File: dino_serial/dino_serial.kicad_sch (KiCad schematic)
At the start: 0 parts

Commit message: feat: phase G on silicon -- serial card, 9600 8N1, echo proven
The PC16550D card (U101 '138, U102 '245, U103, dino_serial/) runs on the
bench. Every step-4..8 witness passed 2026-09-04: serid 0x55, serid_aa
0xAA, serlsr 0x60, seriir 0xC1, serbaud 153.6 kHz on U103.15, serloop
0x53, sertx "DINO" on the host terminal, serrx echoing a typed character
on OB and back to the host. The data bus is PROVEN, not narrowed: a
receiver DINO does not control decoded it.

Two bench faults found and fixed on the way, both copper, neither
visible to --continuity:
  - the card's ~WR was on U75.5 (an input) instead of U75.6; ~{IO_WR}
    now feeds a real consumer for the first time.
  - C1 was 1uF in the socket against 10uF in the drawing, so the machine
    had no power-on reset: reset released ~1ms into the rail ramp and the
    UART started un-reset, framing 5-bit characters until the button
    gave it its first real MR. 10uF fitted; cold boot is clean. New rule
    in CLAUDE.md: a component value is copper too.

Tooling:
  - progrom_gen.Unoracled: the oracle's by-design refusals (non-SCR UART
    registers, undefined carry) are a subclass; asm.py --run reports them
    and still writes the image instead of dying in make burn-prog-*.
    roms_readme_gen lists such images as UNORACLED.
  - docs/notes/serprobe_host.py: stdlib host probe, sends bytes and prints
    every returned byte in hex with timing. Replaces the terminal as the
    serial witness.
  - docs/notes/test_serial_card.py: the card schematic's paper witness.
  - Makefile: make monitor / kill-monitor.

Images: the eight phase G witnesses, five diagnostics from the cold-boot
chase (serrx0, serlcr, serlive, serrxlcr, serrxlive), and the phase F
coverage ROMs that were on disk but never committed.

Co-Authored-By: Claude Fable 5.1 <noreply@anthropic.com>
Claude-Session: https://claude.ai/code/session_01WMy1UioY1p8BufsC2zZ3hR
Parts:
- added C1, C2, C3: 0.1µF, symbol Device:C_Small
- added J1: FTDI I/O, symbol Connector:Conn_01x06_Socket
- added U101: 74LS138, symbol 74xx:74LS138
- added U102: 74LS245, symbol 74xx:74LS245
- added U103: 16550, Package_DIP:DIP-40_W15.24mm, symbol Interface_UART:16550
- added Y1: 3.6864MHz, Oscillator:Oscillator_DIP-8, symbol Oscillator:CXO_DIP8
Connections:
- new net +5V: C1.1, C2.1, C3.1, U101.16 (VCC), U101.6 (E3), U102.20 (VCC), U103.12 (CS0), U103.13 (CS1), U103.36 (~{CTS}), U103.37 (~{DSR}), U103.38 (~{DCD}), U103.39 (~{RI}), U103.40 (VCC), Y1.1 (EN), Y1.8 (Vcc)
- new net GND: C1.2, C2.2, C3.2, J1.1 (Pin_1), U101.5 (E2), U101.8 (GND), U102.10 (GND), U103.19 (WR), U103.20 (GND), U103.22 (RD), U103.25 (~{ADS}), Y1.4 (GND)
- new net M0: U103.28 (A0)
- new net M1: U103.27 (A1)
- new net M11: U101.1 (A0)
- new net M12: U101.2 (A1)
- new net M13: U101.3 (A2)
- new net M2: U103.26 (A2)
- new net RESET_B: U103.35 (MR)
- new net RXD: J1.4 (Pin_4), U103.11 (SOUT)
- new net SD0: U102.18 (B0), U103.1 (D0)
- new net SD1: U102.17 (B1), U103.2 (D1)
- new net SD2: U102.16 (B2), U103.3 (D2)
- new net SD3: U102.15 (B3), U103.4 (D3)
- new net SD4: U102.14 (B4), U103.5 (D4)
- new net SD5: U102.13 (B5), U103.6 (D5)
- new net SD6: U102.12 (B6), U103.7 (D6)
- new net SD7: U102.11 (B7), U103.8 (D7)
- new net SERDIR: U102.1 (DIR), U103.23 (DDIS)
- new net SIN: J1.3 (Pin_3), U103.10 (SIN)
- new net W0: U102.2 (A0)
- new net W1: U102.3 (A1)
- new net W2: U102.4 (A2)
- new net W3: U102.5 (A3)
- new net W4: U102.6 (A4)
- new net W5: U102.7 (A5)
- new net W6: U102.8 (A6)
- new net W7: U102.9 (A7)
- new net XIN: U103.16 (XIN), Y1.5 (OUT)
- new net ~{BAUDOUT}: U103.15 (~{BAUDOUT}), U103.9 (RCLK)
- new net ~{IO_RD_Q}: U103.21 (~{RD})
- new net ~{IO_SEL}: U101.4 (E1)
- new net ~{IO_WR}: U103.18 (~{WR})
- new net ~{SER_SEL}: U101.14 (O1), U102.19 (CE), U103.14 (~{CS2})
- no-connect marks 0 -> 18
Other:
- title: (none) -> Dino Serial Card

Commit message: feat(pcb): started PCB — mainboard DRC clean, placer tools, serial card footprints
Mainboard (dino_v0_0_2): GND zones on both layers re-parameterised to
0.25 mm clearance / 0.2 mm min width so the pour threads the channels
the router spaced for 0.25 mm tracks; 43 GND jump vias and one F.Cu
rule area (J6 pad 50) clear the starved-thermal reports. kicad-cli DRC:
0 unconnected, 0 clearance, 0 shorts; silk warnings only. Project zone
defaults and via size follow.

docs/notes/pcb_tools: the placement scripts from the 2026-09-12 layout
session (anneal.py simulated-annealing cell placer, hpwl.py, report.py,
place_sheetrows.py), promoted verbatim from a session scratchpad so the
DMA/INT re-shuffle can reuse them. Throwaway quality; README says how.

dino_serial: footprints assigned to all six parts, card PCB started.

Co-Authored-By: Claude Opus 5 <noreply@anthropic.com>
Claude-Session: https://claude.ai/code/session_01Qfuso4zXCFF2iuVHgVo7c8
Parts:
- C1, C2, C3: footprint (none) -> Capacitor_THT:C_Disc_D10.0mm_W2.5mm_P5.00mm
- J1: footprint (none) -> Connector_PinSocket_2.54mm:PinSocket_1x06_P2.54mm_Vertical
- U101: footprint (none) -> Package_DIP:DIP-16_W7.62mm
- U102: footprint (none) -> Package_DIP:DIP-20_W7.62mm
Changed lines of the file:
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@@
 			)
 		)
-		(property "Footprint" ""
+		(property "Footprint" "Capacitor_THT:C_Disc_D10.0mm_W2.5mm_P5.00mm"
 			(at 58.42 173.99 0)
 			(hide yes)
@@
 			)
 		)
-		(property "Footprint" ""
+		(property "Footprint" "Package_DIP:DIP-20_W7.62mm"
 			(at 80.01 45.72 0)
 			(hide yes)
@@
 			)
 		)
-		(property "Footprint" ""
+		(property "Footprint" "Connector_PinSocket_2.54mm:PinSocket_1x06_P2.54mm_Vertical"
 			(at 262.89 60.96 0)
 			(hide yes)
@@
 			)
 		)
-		(property "Footprint" ""
+		(property "Footprint" "Capacitor_THT:C_Disc_D10.0mm_W2.5mm_P5.00mm"
 			(at 43.18 173.99 0)
 			(hide yes)
@@
 			)
 		)
-		(property "Footprint" ""
+		(property "Footprint" "Capacitor_THT:C_Disc_D10.0mm_W2.5mm_P5.00mm"
 			(at 27.94 173.99 0)
 			(hide yes)
@@
 			)
 		)
-		(property "Footprint" ""
+		(property "Footprint" "Package_DIP:DIP-16_W7.62mm"
 			(at 81.28 104.14 0)
 			(hide yes)

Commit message: feat(int): draw the interrupt block; sheet cleanup pass
New sheet dino_v0_0_2/interrupt.kicad_sch (page 15): U80-U87, R28 4.7k
pull-up on ~{IRQ}, R29 100R on the block's CLK branch, C83-C90. Every
pin per PHASE_INT SECTION 3, checked against the plan with kicad_netlist
and kicad-cli (146 pins, 0 mismatches).

Old sheets (SECTION 3.2): U28.4 lifted off GND to INJECT; U61.3 to
END_OR_ACCEPT; U36.1 to PC_UP_GATED; U49 D0-3 cut from U48 Za-Zd and
routed through U87 as FLAG_NEXT0-3 / FLAG_D0-3; FLAG_C/Z/V/N and the
five decoder outputs made global. dino_serial: U104 74LS05, INTR ->
~{IRQ}, C4.

Placement pass on every sheet: bus entries and global labels no longer
share wires; M, CW, T, IRB and SA buses kept as labelled keys. Nets
diffed against HEAD per sheet: only the intended changes and a rotated
C29. Project ERC: 0 errors. MODULE CONTRACT stamps regenerated.

Co-Authored-By: Claude Fable 5.1 <noreply@anthropic.com>
Claude-Session: https://claude.ai/code/session_01JGxSS4MVUcaZdKZGtKroSg
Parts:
- added C4: 0.1µF, Capacitor_THT:C_Disc_D5.0mm_W2.5mm_P2.50mm, symbol Device:C_Small
- added U104: 74LS05, Package_DIP:DIP-14_W7.62mm, symbol 74xx:74LS05
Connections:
- net +5V: now also C4.1, U104.14 (VCC)
- net GND: now also C4.2, U104.11, U104.13, U104.3, U104.5, U104.7 (GND), U104.9
- net INTR: now reaches U103.30 (INTR)
- net INTR: now also U104.1
- new net ~{IRQ}: U104.2
- no-connect marks 18 -> 22

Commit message: fix(serial): U104 open-collector inverter is a 7406N, not a 74LS05
No '05 on hand; the '06 is pin-identical (KiCad's 74LS06 extends
74LS05). Netlist identical, ERC unchanged. The 7406N is standard
TTL: INTR sees one full TTL load, ICC up to ~50 mA vs ~6 mA.

Co-Authored-By: Claude Opus 5.5 <noreply@anthropic.com>
Claude-Session: https://claude.ai/code/session_01JGxSS4MVUcaZdKZGtKroSg
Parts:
- U104: value 74LS05 -> 7406N; symbol 74xx:74LS05 -> 74xx:74LS06
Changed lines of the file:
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@@
 	)
 	(symbol
-		(lib_id "74xx:74LS05")
+		(lib_id "74xx:74LS06")
 		(at 114.3 139.7 0)
 		(unit 1)
@@
 			)
 		)
-		(property "Value" "74LS05"
+		(property "Value" "7406N"
 			(at 114.3 133.35 0)
 			(show_name no)
@@
 			)
 		)
-		(property "Datasheet" "http://www.ti.com/lit/gpn/sn74ls05"
+		(property "Datasheet" "http://www.ti.com/lit/gpn/sn7406"
 			(at 114.3 139.7 0)
 			(hide yes)
@@
 			)
 		)
-		(property "Description" "Hex Inverter Open Collector"
+		(property "Description" "Hex Inverter Open Collector, 30 V outputs"
 			(at 114.3 139.7 0)
 			(hide yes)
@@
 	)
 	(symbol
-		(lib_id "74xx:74LS05")
+		(lib_id "74xx:74LS06")
 		(at 114.3 154.94 0)
 		(unit 2)
@@
 			)
 		)
-		(property "Value" "74LS05"
+		(property "Value" "7406N"
 			(at 114.3 148.59 0)
 			(show_name no)
@@
 			)
 		)
-		(property "Datasheet" "http://www.ti.com/lit/gpn/sn74ls05"
+		(property "Datasheet" "http://www.ti.com/lit/gpn/sn7406"
 			(at 114.3 154.94 0)
 			(hide yes)
@@
 			)
 		)
-		(property "Description" "Hex Inverter Open Collector"
+		(property "Description" "Hex Inverter Open Collector, 30 V outputs"
 			(at 114.3 154.94 0)
 			(hide yes)
@@
 	)
 	(symbol
-		(lib_id "74xx:74LS05")
+		(lib_id "74xx:74LS06")
 		(at 114.3 170.18 0)
 		(unit 3)
@@
 			)
 		)
-		(property "Value" "74LS05"
+		(property "Value" "7406N"
 			(at 114.3 163.83 0)
 			(show_name no)
@@
 			)
 		)
-		(property "Datasheet" "http://www.ti.com/lit/gpn/sn74ls05"
+		(property "Datasheet" "http://www.ti.com/lit/gpn/sn7406"
 			(at 114.3 170.18 0)
 			(hide yes)
@@
 			)
 		)
-		(property "Description" "Hex Inverter Open Collector"
+		(property "Description" "Hex Inverter Open Collector, 30 V outputs"
 			(at 114.3 170.18 0)
 			(hide yes)
@@
 	)
 	(symbol
-		(lib_id "74xx:74LS05")
+		(lib_id "74xx:74LS06")
 		(at 149.86 139.7 0)
 		(unit 4)
@@
 			)
 		)
-		(property "Value" "74LS05"
+		(property "Value" "7406N"
 			(at 149.86 133.35 0)
 			(show_name no)
@@
 			)
 		)
-		(property "Datasheet" "http://www.ti.com/lit/gpn/sn74ls05"
+		(property "Datasheet" "http://www.ti.com/lit/gpn/sn7406"
 			(at 149.86 139.7 0)
 			(hide yes)
@@
 			)
 		)
-		(property "Description" "Hex Inverter Open Collector"
+		(property "Description" "Hex Inverter Open Collector, 30 V outputs"
 			(at 149.86 139.7 0)
 			(hide yes)
@@
 	)
 	(symbol
-		(lib_id "74xx:74LS05")
+		(lib_id "74xx:74LS06")
 		(at 149.86 154.94 0)
 		(unit 5)
@@
 			)
 		)
-		(property "Value" "74LS05"
+		(property "Value" "7406N"
 			(at 149.86 148.59 0)
 			(show_name no)
@@
 			)
 		)
-		(property "Datasheet" "http://www.ti.com/lit/gpn/sn74ls05"
+		(property "Datasheet" "http://www.ti.com/lit/gpn/sn7406"
 			(at 149.86 154.94 0)
 			(hide yes)
@@
 			)
 		)
-		(property "Description" "Hex Inverter Open Collector"
+		(property "Description" "Hex Inverter Open Collector, 30 V outputs"
 			(at 149.86 154.94 0)
 			(hide yes)
@@
 	)
 	(symbol
-		(lib_id "74xx:74LS05")
+		(lib_id "74xx:74LS06")
 		(at 149.86 170.18 0)
 		(unit 6)
@@
 			)
 		)
-		(property "Value" "74LS05"
+		(property "Value" "7406N"
 			(at 149.86 163.83 0)
 			(show_name no)
@@
 			)
 		)
-		(property "Datasheet" "http://www.ti.com/lit/gpn/sn74ls05"
+		(property "Datasheet" "http://www.ti.com/lit/gpn/sn7406"
 			(at 149.86 170.18 0)
 			(hide yes)
@@
 			)
 		)
-		(property "Description" "Hex Inverter Open Collector"
+		(property "Description" "Hex Inverter Open Collector, 30 V outputs"
 			(at 149.86 170.18 0)
 			(hide yes)
@@
 	)
 	(symbol
-		(lib_id "74xx:74LS05")
+		(lib_id "74xx:74LS06")
 		(at 185.42 154.94 0)
 		(unit 7)
@@
 			)
 		)
-		(property "Value" "74LS05"
+		(property "Value" "7406N"
 			(at 185.42 148.59 0)
 			(show_name no)
@@
 			)
 		)
-		(property "Datasheet" "http://www.ti.com/lit/gpn/sn74ls05"
+		(property "Datasheet" "http://www.ti.com/lit/gpn/sn7406"
 			(at 185.42 154.94 0)
 			(hide yes)
@@
 			)
 		)
-		(property "Description" "Hex Inverter Open Collector"
+		(property "Description" "Hex Inverter Open Collector, 30 V outputs"
 			(at 185.42 154.94 0)
 			(hide yes)

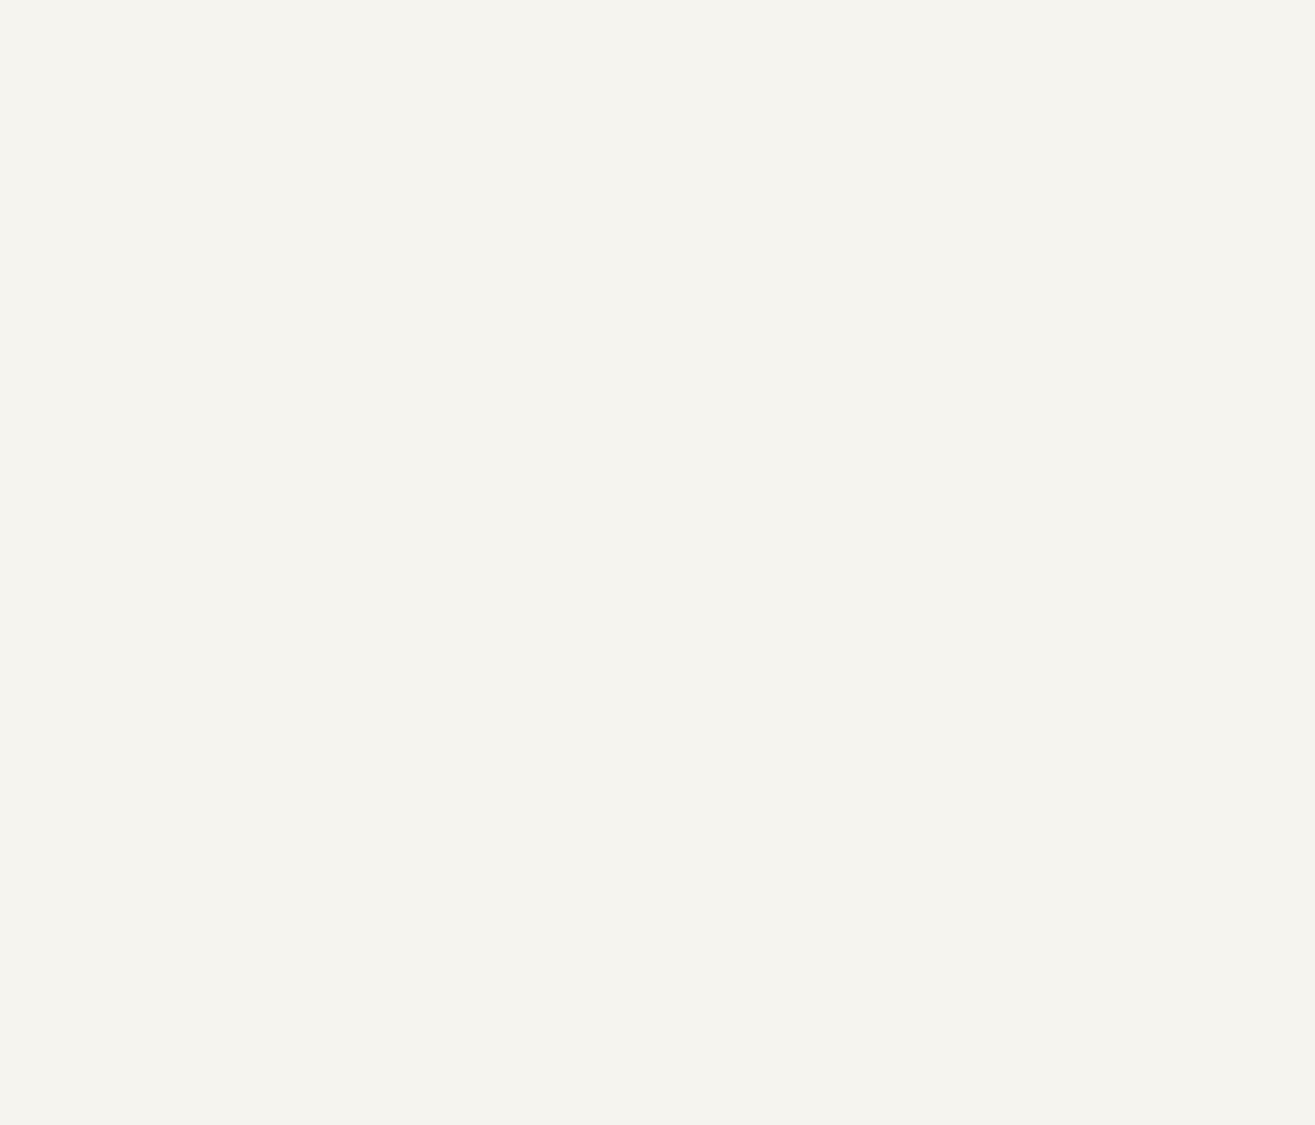
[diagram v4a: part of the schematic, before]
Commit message: feat(fpga): FPGA twin with slots J1-J8 and one card API
A net-new FPGA twin, the third twin beside the breadboard and netsim:
the Rev 1.0 mainboard and its cards as synthesizable Verilog, one
instance per chip by pin number from the same KiCad netlists, on a
48 MHz clk_sys (CLK 1.0 MHz). Runs in Verilator and on the ECP5-5G
Versa (LEDs = OB, DIPs = SW1, UART B19/B12).

Card API: the 37 non-rail pins of bus_gen.BUS, eP_S_xo/_xe in and
_do/_de out, no inout (fpga_twin_gen.py docstring). The mainboard's
J1-J8 are eight copies of it; a slot is a position, not an address.
Separate generators: fpga_core_gen (mainboard only), fpga_card_gen (one
KiCad card), fpga_slots_gen (the slot table -> dino_system), registry
fpga_cards (source, window, oracle model). Hand-written cards start
from fpga/cards/proto_card.v ('138 on M11-M13, ~IO_SEL, W on
~IO_RD_Q). Slots: J1 card zero, J2 serial, J3 DEADBEEF (RTL, 0x5000).

- dino_serial: J2 DINO_BUS_EDGE drawn (Konnect); netlist otherwise
  unchanged, ERC 34 -> 3 (pre-existing warnings)
- oracle: simulate(cards=...) sees the slot table; empty = unchanged
- asm/deadbeef.asm: 0x5A with the card, 0xE1-0xE7 names the failing read
- make fpga-twin: 44 images x 3 seeds, 132/132, no contention; every
  pre-existing result byte-identical to before the slot rewrite
- Versa: PROG_deadbeef 0x5A on the LEDs; earlier isa 0xB4, imon,
  SCELBAL 11/11 sessions identical to the 8008 (echo-paced)
- tests: test_fpga_twin 32/32, test_fpga_slots 37/37, 17 planted faults
  caught; host suite 725 passed
- asm/diploop, asm/swecho: live DIP images for the Versa

Co-Authored-By: Claude Opus 5.5 <noreply@anthropic.com>
Claude-Session: https://claude.ai/code/session_01WWrg3G2ctZoH9upbPMfGmw
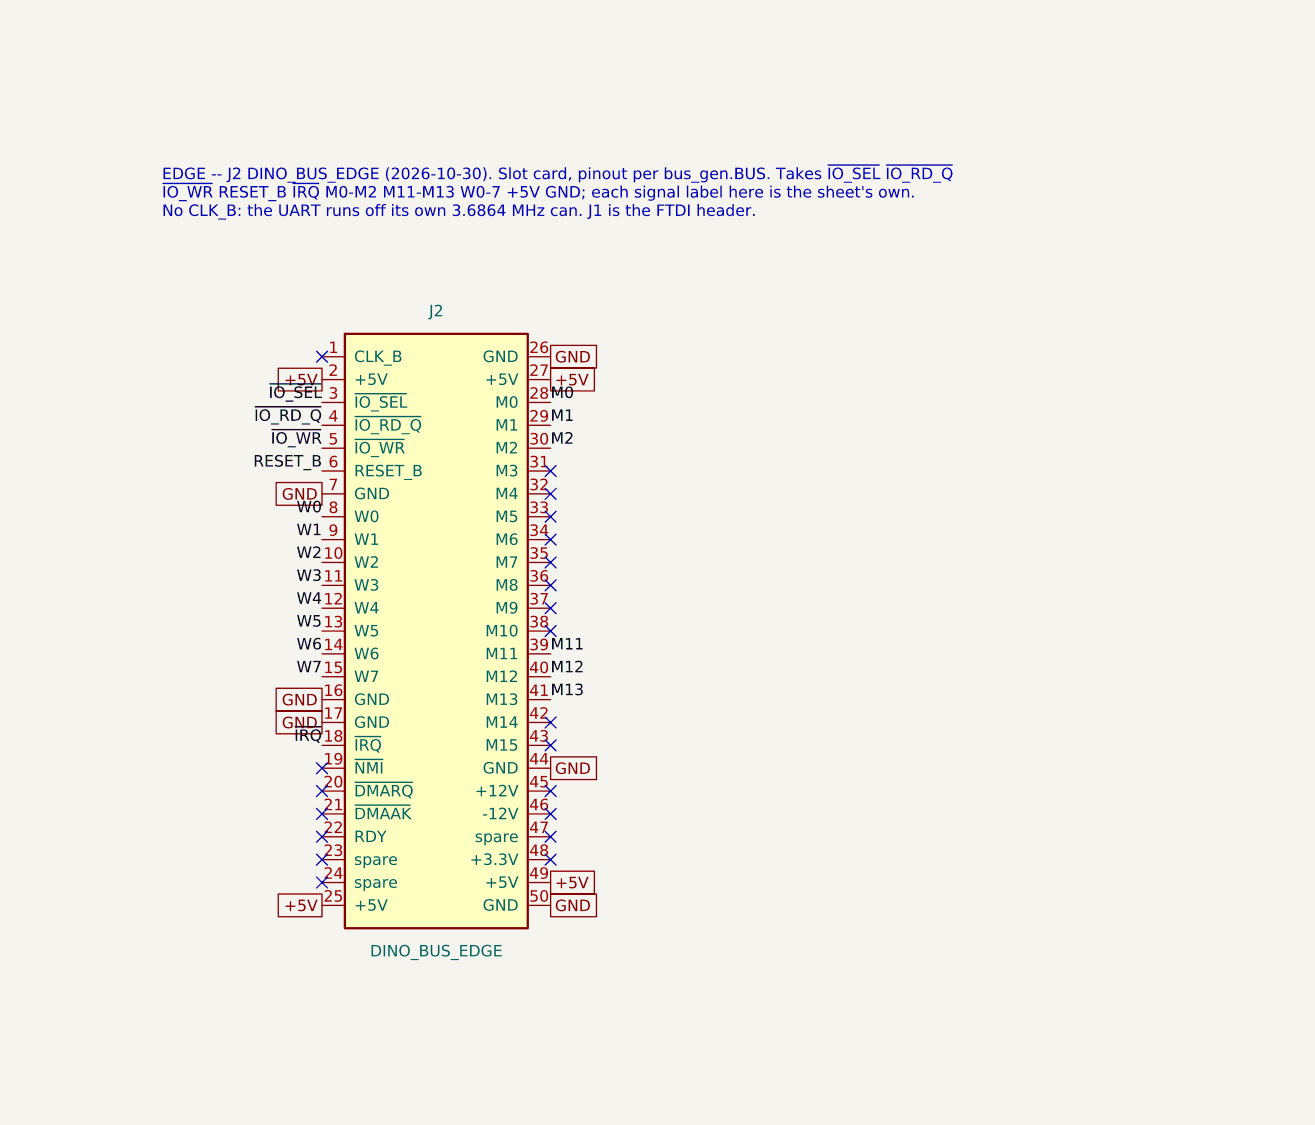
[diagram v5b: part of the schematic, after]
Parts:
- added J2: DINO_BUS_EDGE, dino_bus:EdgeFingers_2x25_P2.54mm, symbol dino_bus:DINO_BUS_EDGE
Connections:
- net +5V: now also J2.2 (+5V), J2.25 (+5V), J2.27 (+5V), J2.49 (+5V)
- net GND: now also J2.16 (GND), J2.17 (GND), J2.26 (GND), J2.44 (GND), J2.50 (GND), J2.7 (GND)
- net M0: now also J2.28 (M0)
- net M1: now also J2.29 (M1)
- net M11: now also J2.39 (M11)
- net M12: now also J2.40 (M12)
- net M13: now also J2.41 (M13)
- net M2: now also J2.30 (M2)
- net RESET_B: now also J2.6 (RESET_B)
- net W0: now also J2.8 (W0)
- net W1: now also J2.9 (W1)
- net W2: now also J2.10 (W2)
- net W3: now also J2.11 (W3)
- net W4: now also J2.12 (W4)
- net W5: now also J2.13 (W5)
- net W6: now also J2.14 (W6)
- net W7: now also J2.15 (W7)
- net ~{IO_RD_Q}: now also J2.4 (~{IO_RD_Q})
- net ~{IO_SEL}: now also J2.3 (~{IO_SEL})
- net ~{IO_WR}: now also J2.5 (~{IO_WR})
- net ~{IRQ}: now also J2.18 (~{IRQ})
- no-connect marks 22 -> 43
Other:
- note added: "EDGE -- J2 DINO_BUS_EDGE (2026-10-30). Slot card, pinout per bus_gen.BUS. Takes ~{IO_SEL} ~{IO_RD_Q} ~{IO_WR} RESET_B ~{IRQ} M0-M2 M11-M13 W0-7 +5V GND; each signal label here is the sheet's own. No CLK_B: the UART runs off its own 3.6864 MHz can. J1 is the FTDI header."
